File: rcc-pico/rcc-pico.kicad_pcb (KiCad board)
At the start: 2 copper layers, 70 x 55.6 mm, 44 parts, among them J1 PJ-006A, J10 Conn_02x04_Top_Bottom, J2 Screw_Terminal, J3 Conn_03x3_female, J4 Conn_3x4_female, J5 Conn_03x10, J6 Conn_02x04_Top_Bottom, J7 Conn_02x04_Top_Bottom, J8 Conn_3x3_female, J9 Conn_03x9, Q1 BSS138, Q2 BSS138, Q3 BSS138, SW1 SW_Push, U1 AP63300WU-7, U2 AP2115M-3.3TRG1, U4 PicoW

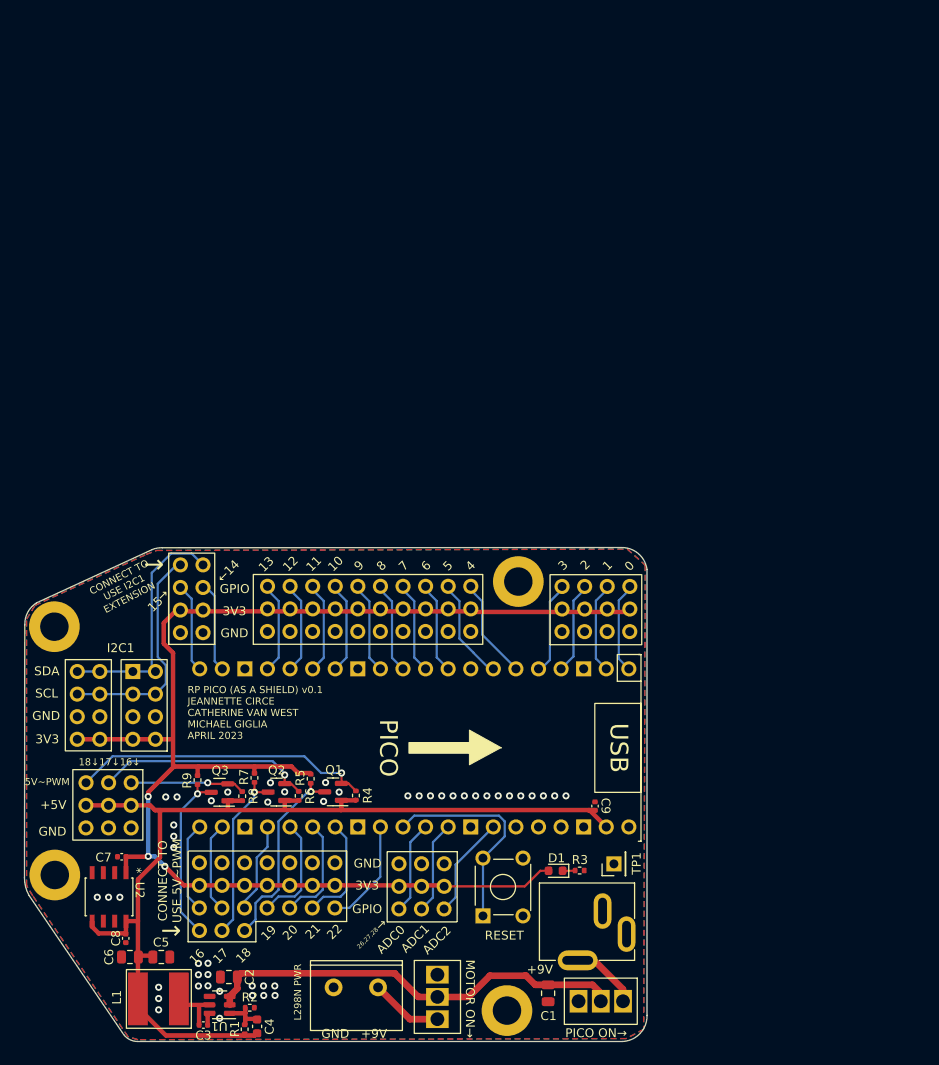
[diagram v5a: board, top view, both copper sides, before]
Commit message: new layout and screenprint
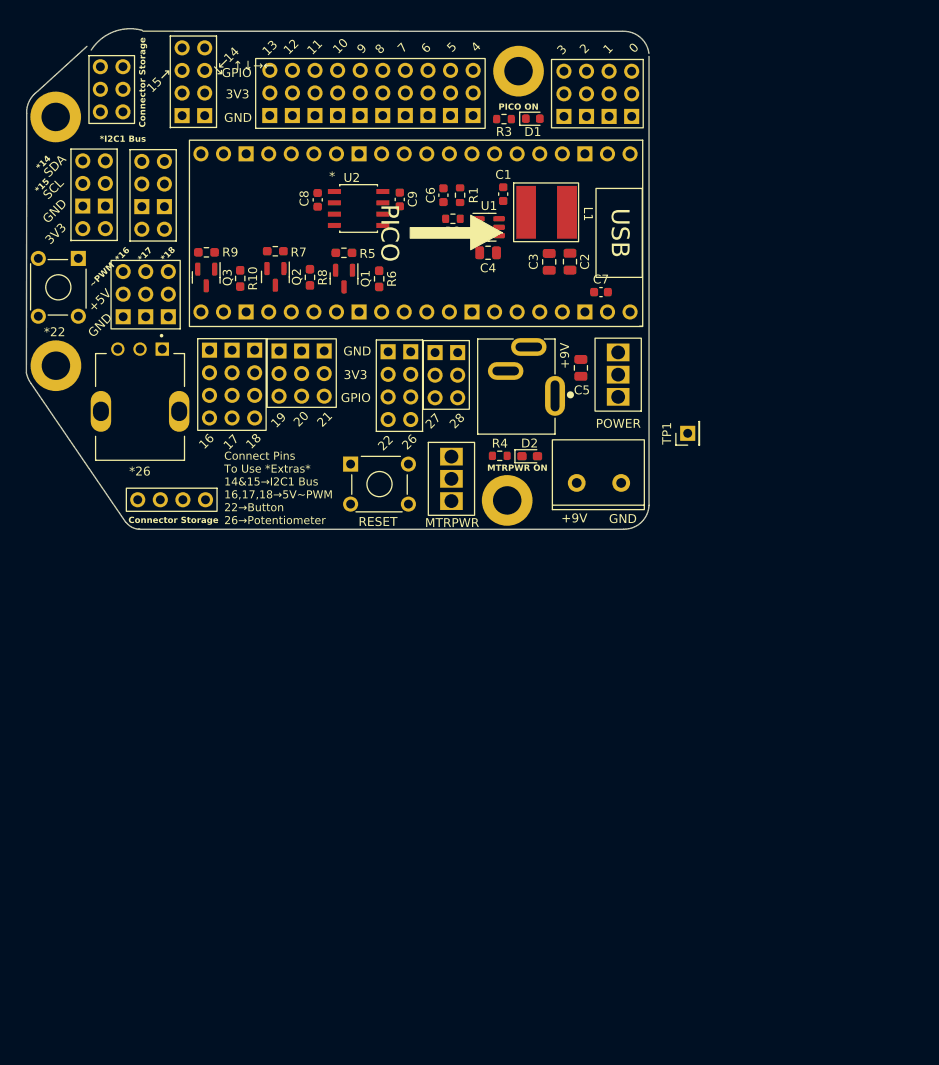
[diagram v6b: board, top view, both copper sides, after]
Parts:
- removed U4: PicoW, 3rdparty:RPi_Pico_SMD_TH
- added D2: LED, LED_SMD:LED_0603_1608Metric_Pad1.05x0.95mm_HandSolder, F.Cu at (133.1, 76.1)
- added J11: Conn_02x04_Odd_Even, PicoShieldHeaders:PinHeader_2x04_P2.54_Vertical_I2C, F.Cu at (84.2, 53.9)
- added J12: Conn_02x04_Odd_Even, PicoShieldHeaders:PinHeader_2x04_P2.54_Vertical_I2C, F.Cu at (90.8, 54.0)
- added J13: ~, PicoShieldHeaders:PinHeader_3x03_P2.54mm_Vertical_Servo, F.Cu at (89.9, 50.3)
- added J14: Conn_02x05_Odd_Even, Connector_PinHeader_2.54mm:PinHeader_2x03_P2.54mm_Vertical, F.Cu at (87.3, 37.4)
- added R10: 10K, Resistor_SMD:R_0603_1608Metric_Pad0.98x0.95mm_HandSolder, F.Cu at (100.5, 56.1)
- added R11: PT01-D120K2-B103, Potentiometer:TRIM_PT01-D120K2-B103, F.Cu at (89.3, 71.1)
- added SW2: SW_Push, Button_Switch_THT:SW_TH_Tactile_Omron_B3F-10xx, F.Cu at (82.3, 53.9)
- added U3: PicoW, PicoShieldHeaders:RPi_Pico_SMD_TH, F.Cu at (120.2, 51.0)
- C1: value 10μ -> 0.1μ; footprint Capacitor_SMD:C_0805_2012Metric -> Capacitor_SMD:C_0603_1608Metric
- C2: value 10μ -> 22μ
- C3: value 0.1μ -> 22μ; footprint Capacitor_SMD:C_0402_1005Metric -> Capacitor_SMD:C_0805_2012Metric
- C4: value 47p -> 10μ; footprint Capacitor_SMD:C_0603_1608Metric -> Capacitor_SMD:C_0805_2012Metric
- C5: value 22μ -> 10μ
- C6: value 22μ -> 47p; footprint Capacitor_SMD:C_0805_2012Metric -> Capacitor_SMD:C_0603_1608Metric
- C7: value 4.7u -> 0.1μ; footprint Capacitor_SMD:C_0402_1005Metric -> Capacitor_SMD:C_0603_1608Metric
- C8: footprint Capacitor_SMD:C_0402_1005Metric -> Capacitor_SMD:C_0603_1608Metric
- C9: value 0.1μ -> 4.7u; footprint Capacitor_SMD:C_0402_1005Metric -> Capacitor_SMD:C_0603_1608Metric
- J1: value PJ-006A -> Conn_02x02_Odd_Even; footprint 3rdparty:CUI_PJ-006A -> Connector_PinSocket_2.54mm:PinSocket_1x04_P2.54mm_Vertical
- J10: value Conn_02x04_Top_Bottom -> Conn_02x04_Odd_Even; footprint Connector_PinHeader_2.54mm:PinHeader_2x04_P2.54mm_Vertical-down -> PicoShieldHeaders:PinHeader_2x04_P2.54_Vertical_I2C_shunt
- J2: value Screw_Terminal -> Conn_02x03_Odd_Even; footprint TerminalBlock:TCxx03_5mm_2x1 -> PicoShieldHeaders:PinHeader_2x03_P2.54mm_Vertical
- J3: value Conn_03x3_female -> PJ-006A; footprint Connector_PinHeader_2.54mm:PinHeader3x3_P2.54mm_Vertical -> PicoShieldHeaders:CUI_PJ-006A
- J4: value Conn_3x4_female -> ~; footprint 3rdparty:PinHeader_3x4_P2.54mm_vertical -> PicoShieldHeaders:PinHeader_3x03_P2.54mm_Vertical_Servo
- J5: value Conn_03x10 -> Conn_3x4_female; footprint 3rdparty:PinHeader_3x11_P2.54mm_Vertical -> PicoShieldHeaders:PinHeader_3x04_P2.54mm_Vertical_gpio
- J6: value Conn_02x04_Top_Bottom -> ~; footprint Connector_PinHeader_2.54mm:PinHeader_2x04_P2.54mm_Vertical -> PicoShieldHeaders:PinHeader_3x04_P2.54mm_Vertical_ServoActivate
- J7: value Conn_02x04_Top_Bottom -> Conn_03x10; footprint Connector_PinHeader_2.54mm:PinHeader_2x04_P2.54mm_Vertical-down -> PicoShieldHeaders:PinHeader_3x11_P2.54mm_Vertical
- J8: value Conn_3x3_female -> Screw_Terminal; footprint Connector_PinHeader_2.54mm:PinHeader3x3_P2.54mm_Vertical -> PicoShieldHeaders:TCxx03_5mm_2x1
- J9: value Conn_03x9 -> Conn_02x04_Odd_Even; footprint 3rdparty:PinHeader3x7+3 -> PicoShieldHeaders:PinHeader_2x04_P2.54_Vertical_I2C_shunt
- L1: footprint Inductor_SMD:BWVS00606045 -> PicoShieldHeaders:BWVS00606045
- R1, R2, R3: footprint Resistor_SMD:R_0402_1005Metric -> Resistor_SMD:R_0603_1608Metric
- R4: value 10K -> 3k; footprint Resistor_SMD:R_0402_1005Metric -> Resistor_SMD:R_0603_1608Metric
- R5, R6, R7, R8, R9: footprint Resistor_SMD:R_0402_1005Metric -> Resistor_SMD:R_0603_1608Metric_Pad0.98x0.95mm_HandSolder
- SW-on/off1, SW-on/off2: footprint 3rdparty:SW-T3-2B-A-A3-S1 -> PicoShieldHeaders:SW-T3-2B-A-A3-S1
- U2: footprint Package_SO:AP2115M-3.3TRG1 -> PicoShieldHeaders:AP2115M-3.3TRG1
- moved H2 112.6 mm to (79.8, 38.0)
- moved H4 104.4 mm to (131.8, 32.8)
- moved R1 96.9 mm to (125.2, 46.8), turned to 90 degrees
- moved C3 94.2 mm to (135.3, 54.2), turned to -90 degrees
- moved C6 92.6 mm to (123.4, 46.8), turned to 90 degrees
- moved U1 92.5 mm to (128.5, 50.4), turned to 0 degrees
- moved R2 91.6 mm to (124.5, 49.4), turned to 180 degrees
- moved C4 90.8 mm to (128.4, 53.2), turned to 0 degrees
- moved L1 90.1 mm to (135.5, 53.8), turned to 0 degrees
- moved C1 90.0 mm to (130.1, 46.6), turned to 90 degrees
- moved C2 89.1 mm to (137.6, 54.2), turned to -90 degrees
- moved C8 85.8 mm to (109.2, 47.3)
- moved R3 84.9 mm to (130.2, 38.2), turned to 180 degrees
- moved D1 84.6 mm to (133.4, 38.1), turned to 0 degrees
- moved C7 83.3 mm to (141.1, 57.6), turned to 0 degrees
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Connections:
- C1 pad 1: +9V -> Net-(U1-BST)
- C1 pad 2: GND -> Net-(U1-SW)
- C2 pad 1: +9V -> +5V
- C3 pad 1: Net-(C3-Pad1) -> +5V
- C3 pad 2: Net-(C3-Pad2) -> GND
- C4 pad 1: Net-(C4-Pad1) -> +9V
- C4 pad 2: +5V -> GND
- C5 pad 1: +5V -> +9V
- C6 pad 1: +5V -> Net-(U1-FB)
- C6 pad 2: GND -> +5V
- C7 pad 1: +3.3V -> GND
- C7 pad 2: GND -> +5V
- C8 pad 1: +5V -> +3.3V
- C9 pad 1: GND -> +5V
- C9 pad 2: +5V -> GND
- J1 pad 1: Net-(J1-Pad1) -> unconnected-(J1-Pin_1-Pad1)
- J1 pad 2: GND -> unconnected-(J1-Pin_2-Pad2)
- J1 pad 3: GND -> unconnected-(J1-Pin_3-Pad3)
- J10 pad 1: /SDA -> /SCL
- J10 pad 2: /SCL -> /SDA
- J10 pad 3: GND -> /GPIO15
- J10 pad 4: +3.3V -> /GPIO14
- J10 pad 5: /SDA -> +3.3V
- J10 pad 6: /SCL -> +3.3V
- J10 pad 8: +3.3V -> GND
- J2 pad 1: /MTRPWR -> GND
- J3 pad 1: GND -> Net-(SW-on/off1-A)
- J4 pad 1: /GPIO0 -> GND
- J4 pad 2: /GPIO1 -> GND
- J4 pad 3: /GPIO2 -> GND
- J4 pad 4: /GPIO3 -> +3.3V
- J4 pad 7: +3.3V -> /GPIO19
- J4 pad 8: +3.3V -> /GPIO20
- J4 pad 9: GND -> /GPIO21
- J5 pad 1: /GPIO4 -> /GPIO0
- J5 pad 10: /GPIO13 -> GND
- J5 pad 11: +3.3V -> GND
- J5 pad 12: +3.3V -> GND
- J5 pad 2: /GPIO5 -> /GPIO1
- J5 pad 3: /GPIO6 -> /GPIO2
- J5 pad 4: /GPIO7 -> /GPIO3
- J5 pad 5: /GPIO8 -> +3.3V
- J5 pad 6: /GPIO9 -> +3.3V
- J5 pad 7: /GPIO10 -> +3.3V
- J5 pad 8: /GPIO11 -> +3.3V
- J5 pad 9: /GPIO12 -> GND
- J6 pad 1: /SCL -> GND
- J6 pad 2: /SDA -> GND
- J6 pad 3: /GPIO15 -> GND
- J6 pad 4: /GPIO14 -> +3.3V
- J6 pad 7: GND -> /GPIO16
- J6 pad 8: GND -> /GPIO17
- J7 pad 1: /SDA -> /GPIO4
- J7 pad 2: /SCL -> /GPIO5
- J7 pad 3: GND -> /GPIO6
- J7 pad 4: +3.3V -> /GPIO7
- J7 pad 5: /SDA -> /GPIO8
- J7 pad 6: /SCL -> /GPIO9
- J7 pad 7: GND -> /GPIO10
- J7 pad 8: +3.3V -> /GPIO11
- J8 pad 1: GND -> /MTRPWR
- J9 pad 1: GND -> /POT_signal
- J9 pad 2: GND -> /extra_button
- J9 pad 3: GND -> /GPIO26
- J9 pad 4: GND -> /GPIO22
- J9 pad 5: GND -> +3.3V
- J9 pad 6: GND -> +3.3V
- J9 pad 8: +3.3V -> GND
- L1 pad 1: Net-(C3-Pad2) -> Net-(U1-SW)
- Q1 pad 1: +5V -> +3.3V
- Q2 pad 1: +5V -> +3.3V
- Q3 pad 1: +5V -> +3.3V
- R1 pad 1: Net-(C4-Pad1) -> Net-(U1-FB)
- R2 pad 1: Net-(C4-Pad1) -> Net-(U1-FB)
- R4 pad 1: +5V -> Net-(D2-K)
- R4 pad 2: /5V_PWM_1 -> GND
- R5 pad 1: +3.3V -> +5V
- R5 pad 2: /3V3_PWM_1 -> /5V_PWM_1
- R6 pad 1: +5V -> +3.3V
- R6 pad 2: /5V_PWM_2 -> /3V3_PWM_1
- R7 pad 1: +3.3V -> +5V
- R7 pad 2: /3V3_PWM_2 -> /5V_PWM_2
- R8 pad 1: +5V -> +3.3V
- R8 pad 2: /5V_PWM_3 -> /3V3_PWM_2
- R9 pad 1: +3.3V -> +5V
- R9 pad 2: /3V3_PWM_3 -> /5V_PWM_3
- SW-on/off1 pad 1: Net-(J1-Pad1) -> Net-(SW-on/off1-A)
- U1 pad 1: Net-(C4-Pad1) -> Net-(U1-FB)
- U1 pad 5: Net-(C3-Pad2) -> Net-(U1-SW)
- U1 pad 6: Net-(C3-Pad1) -> Net-(U1-BST)
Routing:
- net +3.3V: track 160.7 -> 0.00 mm, vias 3 -> 0
- net +5V: track 114.9 -> 0.00 mm
- net +9V: track 48.4 -> 0.00 mm
- net /5V_PWM_1: track 33.9 -> 0.00 mm, vias 1 -> 0
- net /SDA: track 27.2 -> 0.00 mm
- net /SCL: track 24.9 -> 0.00 mm
- net /5V_PWM_2: track 24.4 -> 0.00 mm, vias 1 -> 0
- net /run: track 23.9 -> 0.00 mm
- net /3V3_PWM_1: track 22.4 -> 0.00 mm, vias 1 -> 0
- net /3V3_PWM_2: track 19.7 -> 0.00 mm, vias 1 -> 0
- net /3V3_PWM_3: track 19.7 -> 0.00 mm, vias 1 -> 0
- net /5V_PWM_3: track 12.9 -> 0.00 mm, vias 1 -> 0
- net /GPIO21: track 12.3 -> 0.00 mm
- net /GPIO19: track 12.3 -> 0.00 mm
- net /GPIO22: track 12.2 -> 0.00 mm
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- removed copper zone on B.Cu, net GND
- removed copper zone on F.Cu, net GND
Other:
- board size 70 x 55.6 mm -> 70 x 56.3 mm
- board text added: "*14"
- board text added: "*15"
- board text added: "*16"
- board text added: "*17"
- board text added: "*18"
- board text added: "*22"
- board text added: "*26"
- board text added: "*I2C1 Bus"
- board text added: "26"
- board text added: "27"
- board text added: "28"
- board text added: "Connect Pins To Use *Extras* 14&15→I2C1 Bus 16,17,18→5V~PWM 22→Button 26→Potentiometer"
- board text added: "Connector Storage"
- board text added: "MTRPWR"
- board text added: "MTRPWR ON"
- board text added: "PICO ON"
- board text added: "POWER"
- board text added: "~PWM"
- board text added: "←"
- board text added: "↑↓→←"
- board text removed: "18↓17↓16↓"
- board text removed: "26,27,28"
- board text removed: "5V~PWM"
- board text removed: "ADC0"
- board text removed: "ADC1"
- board text removed: "ADC2"
- board text removed: "BATTERY"
- board text removed: "CONNECT TO USE 5V~PWM"
- board text removed: "CONNECT TO USE I2C1 EXTENSION"
- board text removed: "FRONT"
- board text removed: "GND +9V"
- board text removed: "I2C1"
- board text removed: "L298N"
- board text removed: "L298N PWR"
- board text removed: "MOTOR ON→"
- board text removed: "PICO ON→"
- board text removed: "REAR"
- board text removed: "RP PICO (AS A SHIELD) v0.1 JEANNETTE CIRCE CATHERINE VAN WEST MICHAEL GIGLIA APRIL 2023"
- board text removed: "↓"

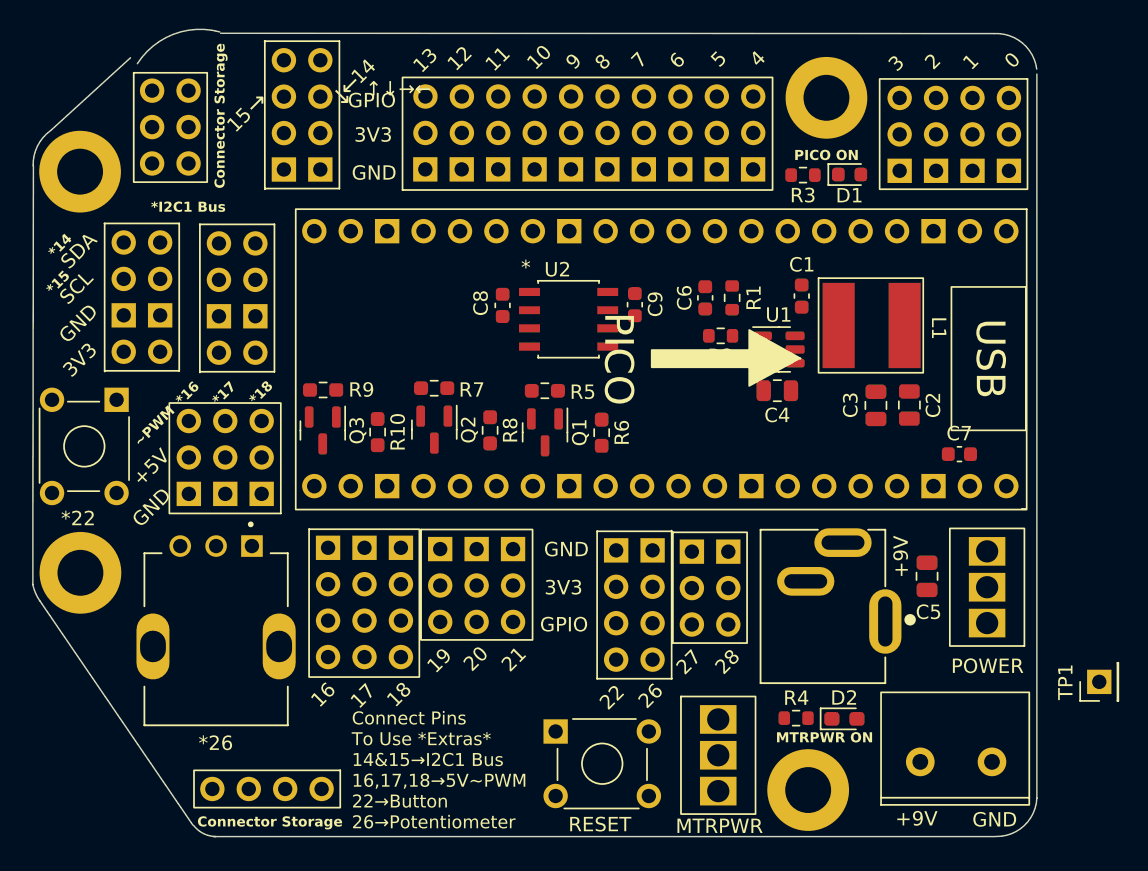
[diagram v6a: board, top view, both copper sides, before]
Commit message: finished traces for v0.2
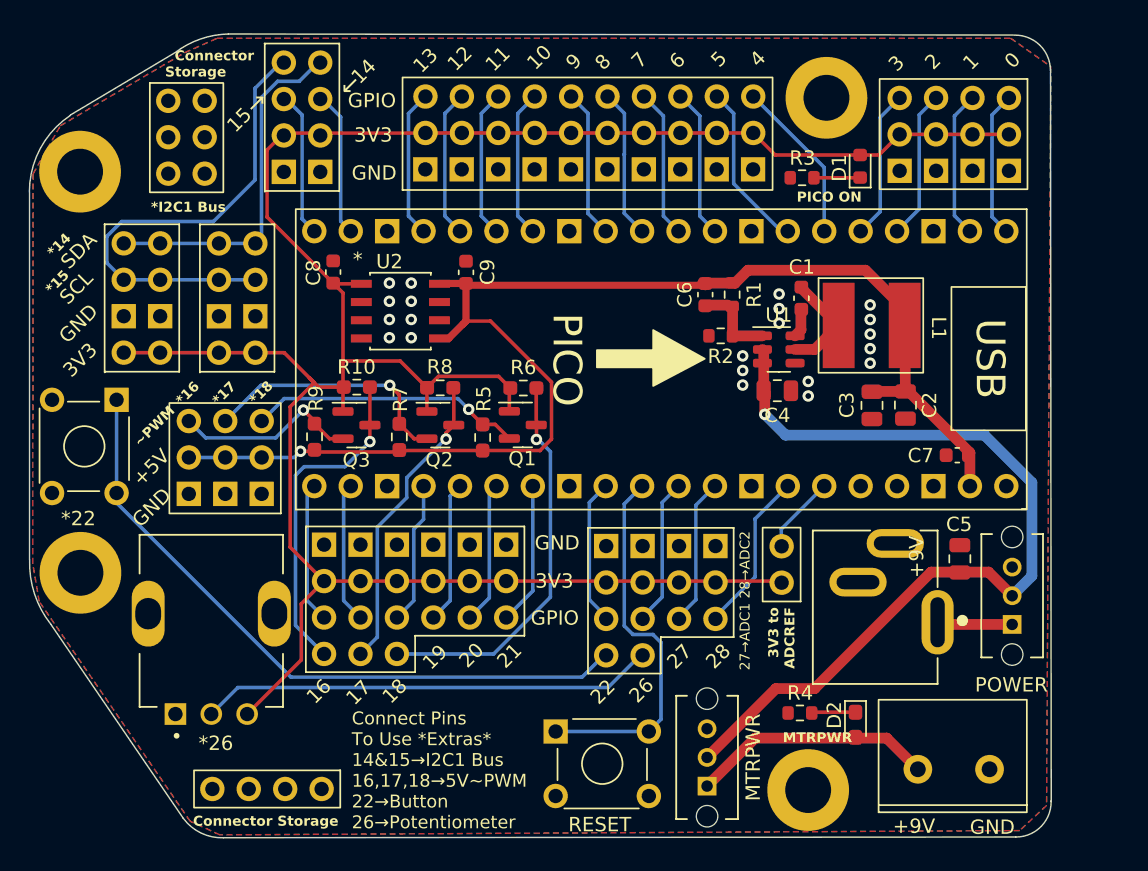
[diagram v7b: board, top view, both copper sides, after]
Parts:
- removed J2: Conn_02x03_Odd_Even, PicoShieldHeaders:PinHeader_2x03_P2.54mm_Vertical
- removed J6: ~, PicoShieldHeaders:PinHeader_3x04_P2.54mm_Vertical_ServoActivate
- removed J9: Conn_02x04_Odd_Even, PicoShieldHeaders:PinHeader_2x04_P2.54_Vertical_I2C_shunt
- removed TP1: TestPoint, Connector_PinHeader_2.54mm:PinHeader_1x01_P2.54mm_Vertical
- added J16: Conn_01x02_Pin, Connector_PinHeader_2.54mm:PinHeader_1x02_P2.54mm_Vertical, F.Cu at (128.7, 64.1)
- added J17: ~, PicoShieldHeaders:Conn_16-21, F.Cu at (100.6, 76.7)
- J4: footprint PicoShieldHeaders:PinHeader_3x03_P2.54mm_Vertical_Servo -> PicoShieldHeaders:Conn_22,24-26
- SW-on/off1, SW-on/off2: footprint PicoShieldHeaders:SW-T3-2B-A-A3-S1 -> PicoShieldHeaders:SW_OS102011MS2QN1
- moved J4 12.9 mm to (120.3, 75.5)
- moved C8 12.0 mm to (97.4, 45.0), turned to 90 degrees
- moved C9 12.0 mm to (106.7, 45.0), turned to 90 degrees
- moved U2 11.7 mm to (102.1, 47.7)
- moved SW-on/off1 6.92 mm to (144.8, 67.5), turned to 90 degrees
- moved R6 6.29 mm to (110.7, 53.0), turned to 0 degrees
- moved SW-on/off2 6.00 mm to (123.5, 78.8), turned to 90 degrees
- moved R5 5.42 mm to (107.8, 56.5), turned to 90 degrees
- moved R8 4.57 mm to (104.9, 53.0), turned to 0 degrees
- moved R7 4.18 mm to (102.0, 56.5), turned to 90 degrees
- moved J3 3.65 mm to (139.6, 69.4)
- moved R10 3.46 mm to (99.1, 53.0), turned to 0 degrees
- moved R9 3.32 mm to (96.1, 56.4), turned to 90 degrees
- moved C5 2.59 mm to (141.1, 65.0)
- moved Q3 2.38 mm to (99.0, 55.6), turned to 0 degrees
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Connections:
- J4 pad 1: GND -> /POT_signal
- J4 pad 2: GND -> /extra_button
- J4 pad 3: GND -> /GPIO26
- J4 pad 4: +3.3V -> /GPIO22
- J4 pad 7: /GPIO19 -> GND
- J4 pad 8: /GPIO20 -> GND
- U3 pad 35: unconnected-(U3-ADC_VREF-Pad35) -> /adcref_3v3
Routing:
- net +3.3V: track 0.00 -> 167.5 mm
- net +5V: track 0.00 -> 91.3 mm, vias 0 -> 1
- net +9V: track 0.00 -> 60.9 mm, vias 0 -> 1
- net /extra_button: track 0.00 -> 46.4 mm
- net /SCL: track 0.00 -> 33.9 mm
- net /POT_signal: track 0.00 -> 31.8 mm
- net /3V3_PWM_1: track 0.00 -> 27.5 mm, vias 0 -> 1
- net /run: track 0.00 -> 26.4 mm
- net /SDA: track 0.00 -> 24.1 mm
- net /3V3_PWM_3: track 0.00 -> 23.2 mm, vias 0 -> 1
- net /3V3_PWM_2: track 0.00 -> 21.2 mm, vias 0 -> 1
- net /5V_PWM_1: track 0.00 -> 19.1 mm, vias 0 -> 1
- net /5V_PWM_2: track 0.00 -> 17.8 mm, vias 0 -> 1
- net /MTRPWR: track 0.00 -> 17.0 mm
- net /5V_PWM_3: track 0.00 -> 12.8 mm, vias 0 -> 1
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- added copper zone on B.Cu, net GND
- added copper zone on F.Cu, net GND
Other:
- board size 70 x 56.3 mm -> 71.3 x 56.1 mm
- board text added: "27→ADC1 28→ADC2"
- board text added: "3V3 to ADCREF"
- board text removed: "MTRPWR ON"
- board text removed: "↑↓→←"

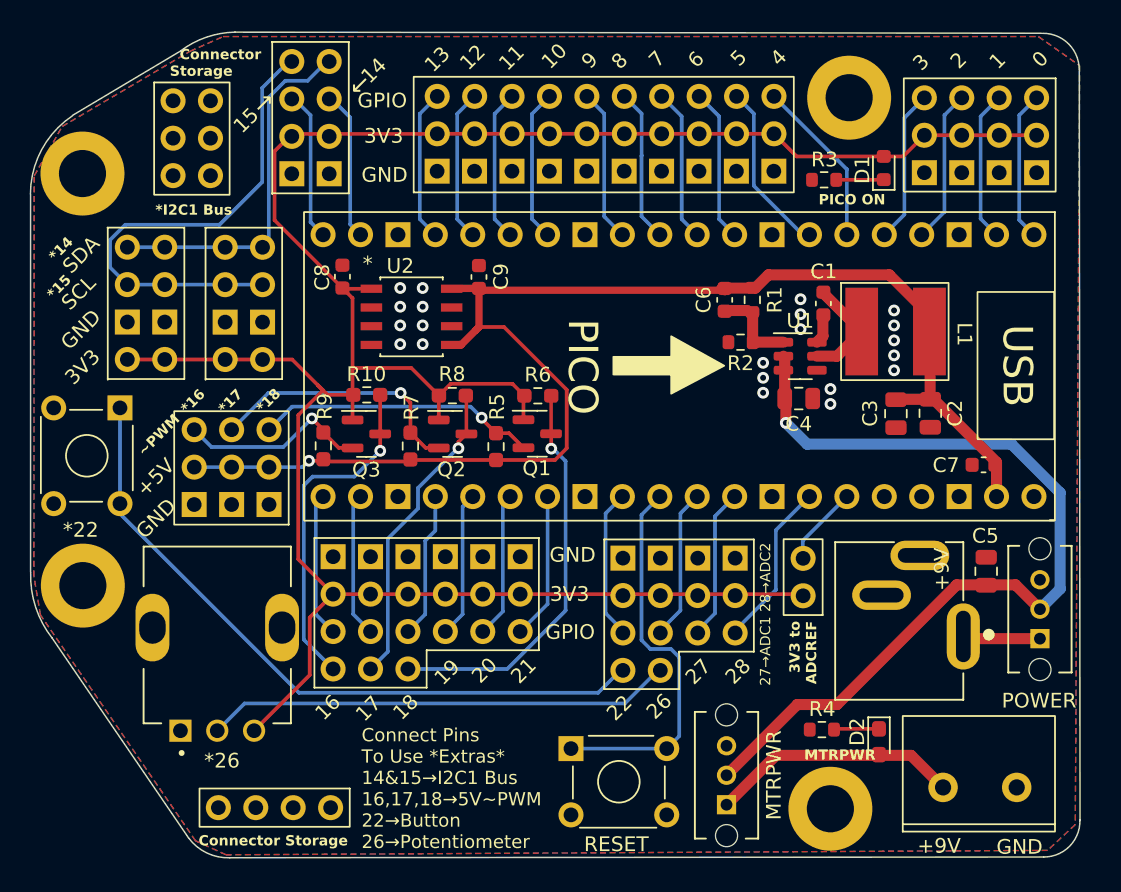
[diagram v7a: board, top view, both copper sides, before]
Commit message: finished DRC, added fiducals and name, cleaned up schematic a bit, still needs some work
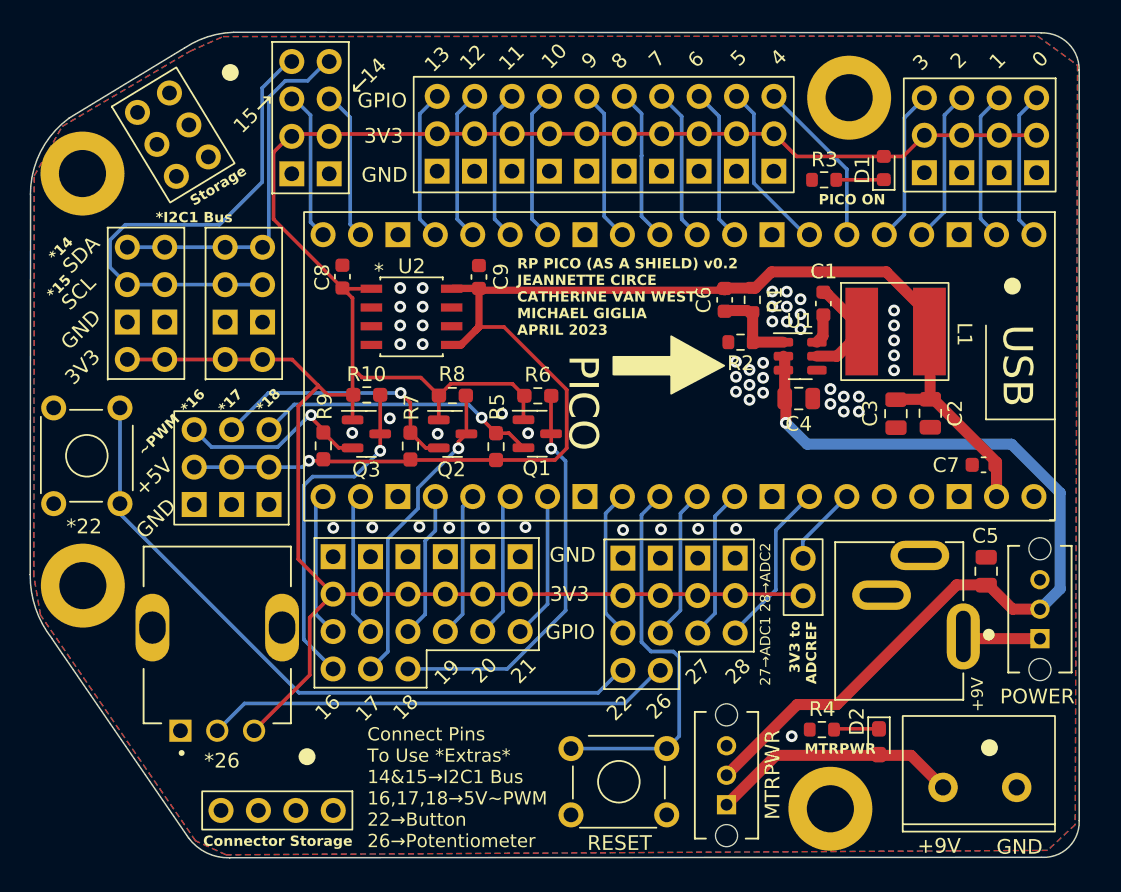
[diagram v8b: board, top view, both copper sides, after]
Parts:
- moved J14 1.28 mm to (88.3, 36.8), turned to -148.7 degrees
- moved J1 0.26 mm to (96.8, 81.2)
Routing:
- net GND: vias 21 -> 53
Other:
- board size 71.3 x 56.1 mm -> 71.2 x 56 mm
- board text added: "RP PICO (AS A SHIELD) v0.2 JEANNETTE CIRCE CATHERINE VAN WEST MICHAEL GIGLIA APRIL 2023"
- board text added: "Storage"
